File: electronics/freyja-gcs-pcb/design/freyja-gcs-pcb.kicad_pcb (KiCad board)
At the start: 4 copper layers, 300 x 200 mm, 306 parts, among them J1 GT-USB-7010ASV, J10 XT60PB-M.G.Y, J11 XT60PB-F.G.Y, J2 JST SR, J3 2x20F, J4 JST SH, J5 JST SH, J6 GT-USB-7010ASV, J7 A2543WR-4P-2, J8 XD-PH-10AW, J9 JS350-S02DCA-00, Q1 TM10N06SI, Q10 NPN, Q11 NPN, Q12 NPN, Q13 NPN, Q14 NPN, Q15 NPN, Q16 NPN, Q17 NPN, Q18 NPN, Q19 NPN, Q2 TM10N06SI, Q20 NPN, Q21 NPN, Q22 NPN, Q23 NPN, Q24 AO4459, Q25 AO4459, Q26 NPN, Q3 AO4459, Q4 L2N7002SLLT1G, Q5 L2N7002SLLT1G, Q6 TM10N06SI, Q7 TM10N06SI, Q8 TM10N06SI, Q9 NPN, SW1 SW_SPST, SW10 PB22E09071, SW11 ST-0-102-A01-T000-LF+PJ, SW12 ST-0-102-A01-T000-LF+PJ, SW13 ST-0-102-A01-T000-LF+PJ, SW14 ST-0-102-A01-T000-LF+PJ, SW2 SW_SPST, SW3 K6-6136D-L1-04, SW4 PB22E09071, SW5 ST-0-102-A01-T000-LF+PJ, SW6 ST-0-102-A01-T000-LF+PJ, SW7 PB22E09071, SW8 ST-0-102-A01-T000-LF+PJ, SW9 ST-0-102-A01-T000-LF+PJ, U1 STM32U575RGTx, U10 LM74700QDBVRQ1, U11 AMS1117-3.3, U12 RY3730, U13 74HC595, U14 74HC595, U2 SN65HVD232DR, U3 FM7021DB, U4 CN3702, U5 HY2213-BB3A, U6 HY2213-BB3A, U7 IP2721, U8 SY8368AQQC, U9 LM74700QDBVRQ1, Y1 48MHz, Y2 32768Hz

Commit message: fix footprints
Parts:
- removed the G*** at (221.0, 124.0)

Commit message: aesir logo
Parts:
- added G***: LOGO, prjlib:aesir_logo_large, F.Cu at (221.5, 124.0)

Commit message: dnp logos
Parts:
- renumbered G*** to LOGO1, G*** to LOGO2
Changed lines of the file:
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@@
 		(layer "F.Cu")
 		(at 221.5 124)
-		(property "Reference" "G***"
+		(property "Reference" "LOGO1"
 			(at 0 0 0)
 			(layer "F.SilkS")
@@
 			)
 		)
-		(attr through_hole)
+		(attr through_hole board_only exclude_from_pos_files exclude_from_bom dnp)
 		(fp_poly
 			(pts
@@
 		(layer "B.Cu")
 		(at 172 122 180)
-		(property "Reference" "G***"
+		(property "Reference" "LOGO2"
 			(at 0 0 0)
 			(layer "B.SilkS")
@@
 			)
 		)
-		(attr board_only exclude_from_pos_files exclude_from_bom)
+		(attr board_only exclude_from_pos_files exclude_from_bom dnp)
 		(fp_poly
 			(pts

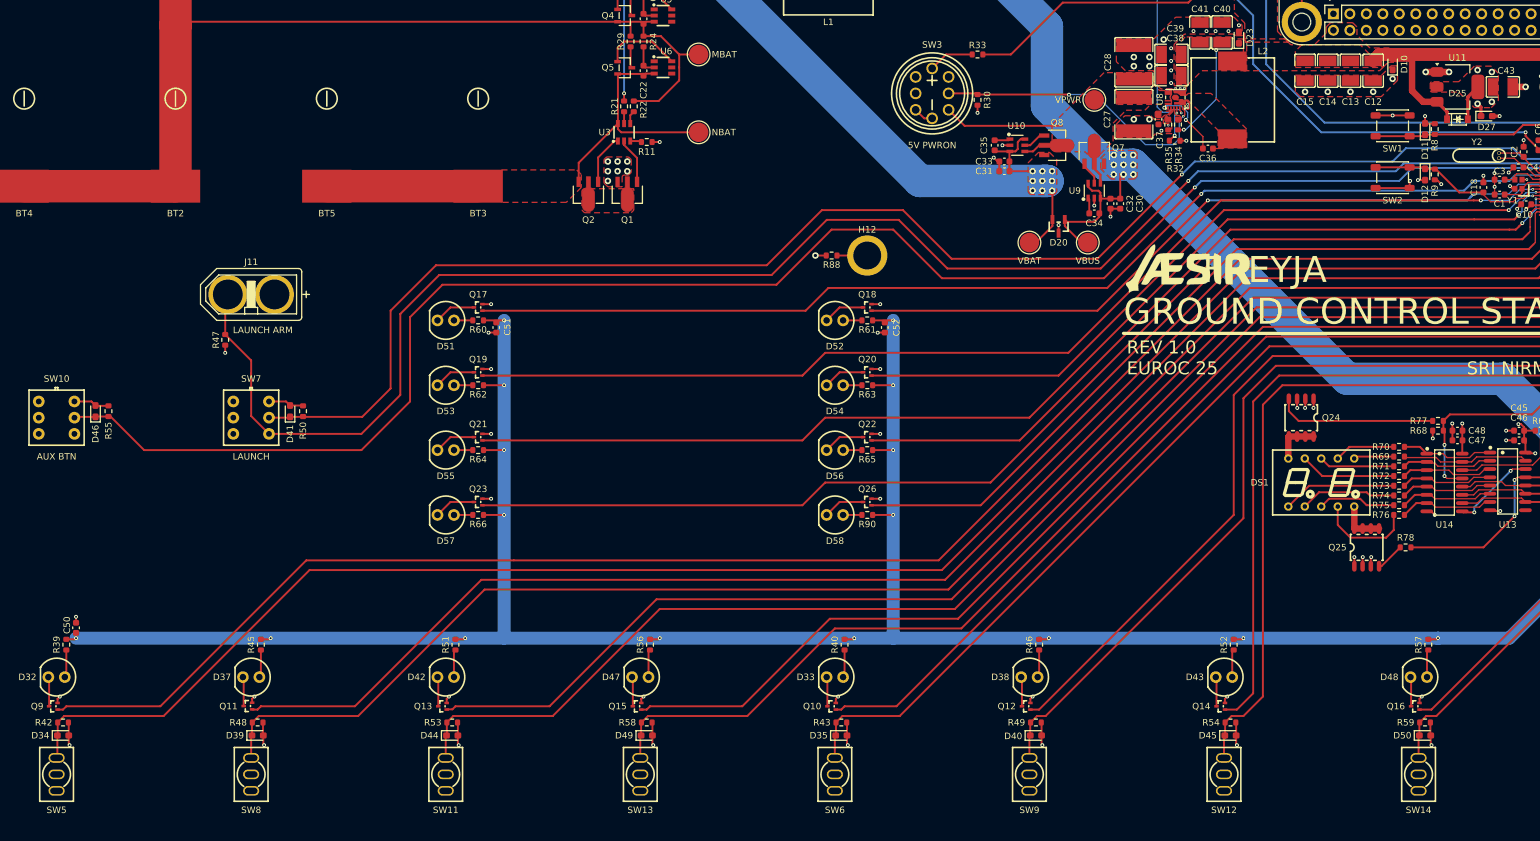
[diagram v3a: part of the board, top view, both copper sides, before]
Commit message: change to available parts
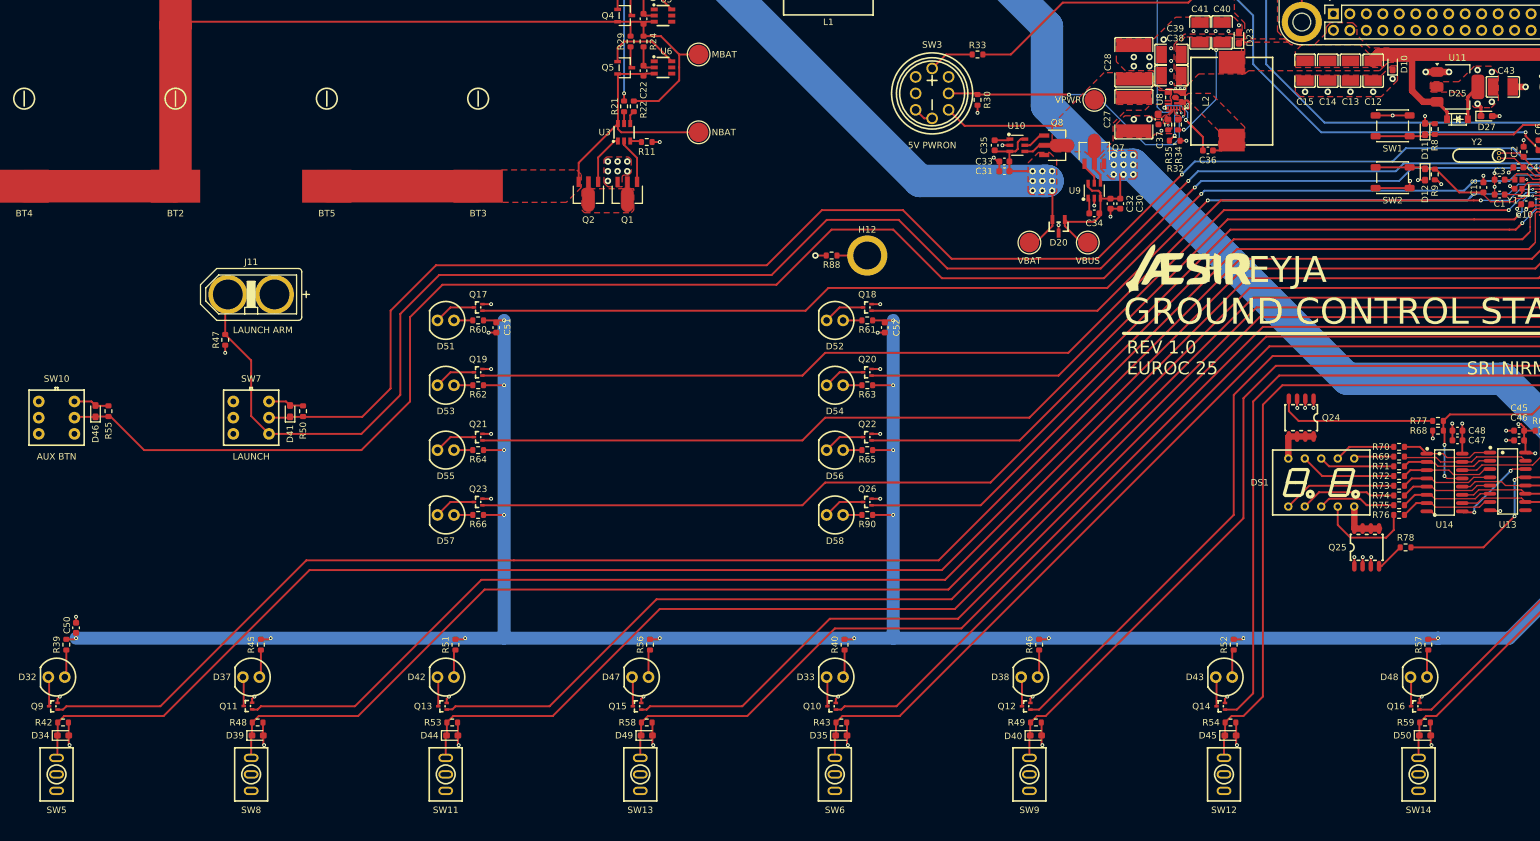
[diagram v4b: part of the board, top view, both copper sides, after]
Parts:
- L2: footprint EasyEDA:IND-SMD_L13.5-W12.8 -> EasyEDA:IND-SMD_L13.5-W12.6
- Q1, Q2, Q6, Q7, Q8: value TM10N06SI -> XR15N06Q
- SW11, SW12, SW13, SW14, SW5, SW6, SW8, SW9: value ST-0-102-A01-T000-LF+PJ -> 2MS1T1B1M2QES; footprint EasyEDA:SW-TH_3P-L8.3-W5.2-P2.54_ST-0-102-A01-T000 -> EasyEDA:SW-TH_2MS1T1B1M2QES-5
- moved C36 0.30 mm to (224.5, 105.8)
- moved L2 0.22 mm to (228.2, 98.2), turned to 90 degrees
- turned SW11 to 0 degrees
- turned SW12 to 0 degrees
- turned SW13 to 0 degrees
- turned SW14 to 0 degrees
- turned SW5 to 0 degrees
- turned SW6 to 0 degrees
- turned SW8 to 0 degrees
- turned SW9 to 0 degrees
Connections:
- net VBUS renamed /Power/VBUS
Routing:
- net Net-(U8-BS): track 11.6 -> 15.5 mm
